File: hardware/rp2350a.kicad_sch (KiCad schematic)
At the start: 51 parts, among them Q2 DMN1150UFB-7B, Q7 DMN1150UFB-7B, U10 TXU0101DRYR, U32 TS2306A 240GF MSM 9_C2976675, U36 RP2354B_C39843328, X1 XTM25012000JT00351001

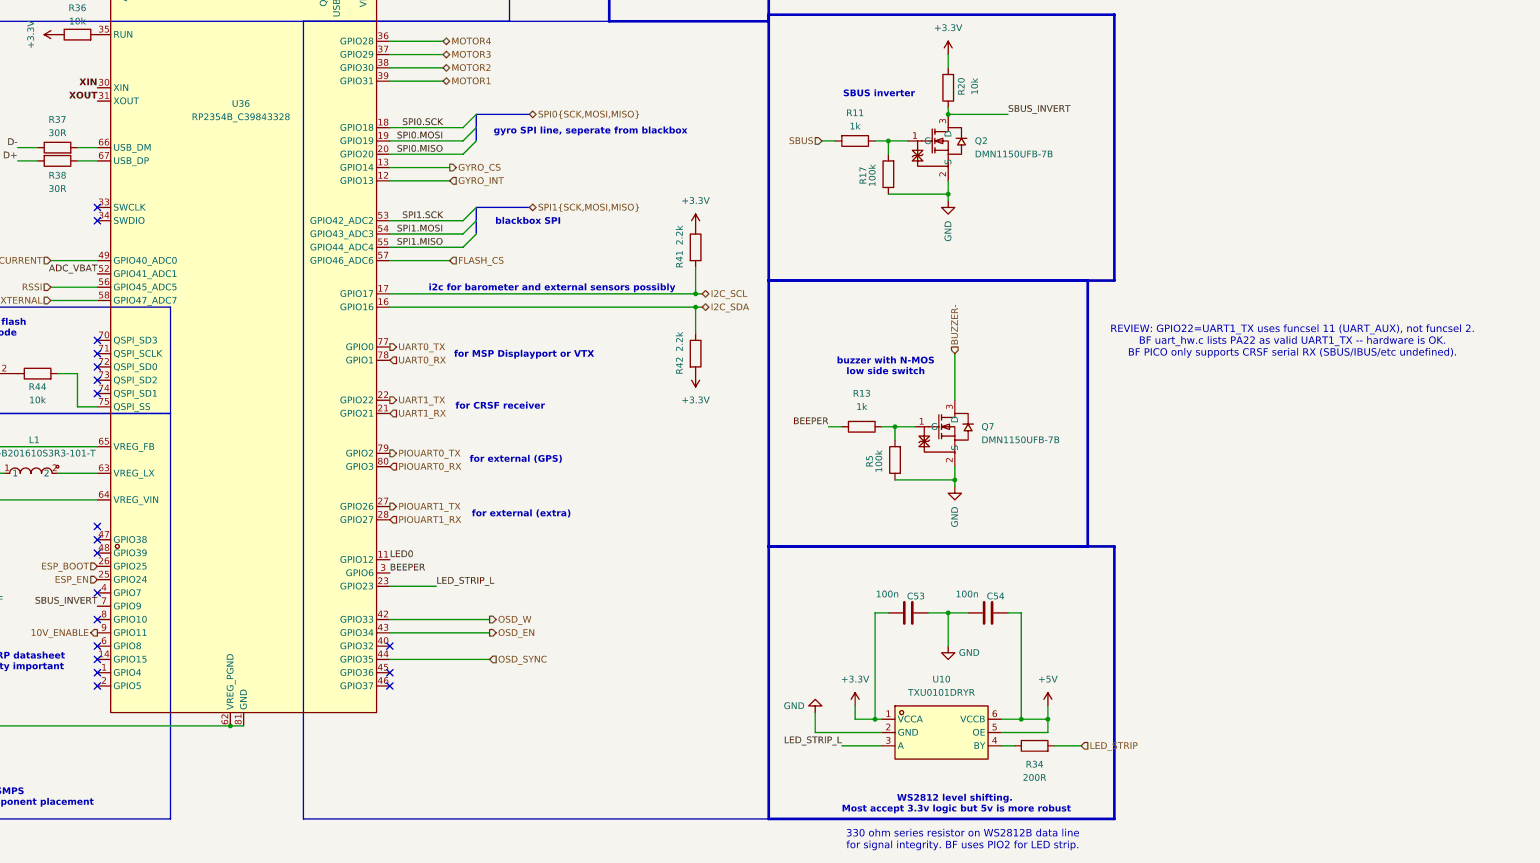
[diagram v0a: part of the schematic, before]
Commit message: Standardize repo: .gitignore, README, license, remove orphaned files
- Standardize .gitignore to match ecosystem template
- Fix README: correct GitHub URL, remove generic sections, remove nonexistent dirs
- Replace LICENSE stub with full CERN-OHL-S-2.0 text
- Remove orphaned schematics (baro, blackbox, compass, elrs, leds) — not in ECO variant
- Delete self-referential symlink and parent OpenFC production leftovers
- Add new footprints and 3D models (SIM, TF connectors)

Co-Authored-By: Claude Opus 4.6 (1M context) <noreply@anthropic.com>
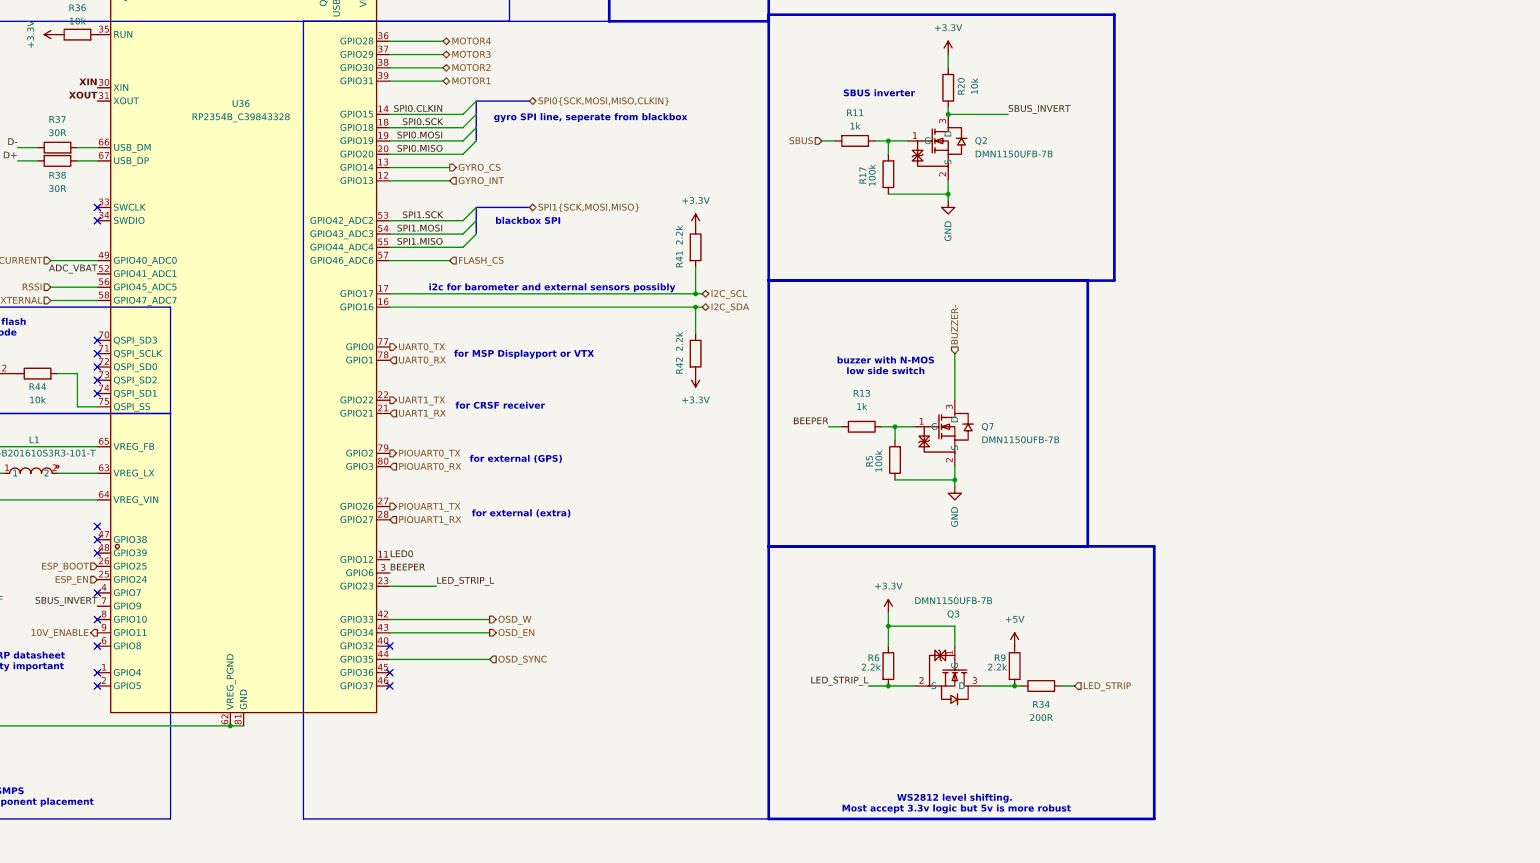
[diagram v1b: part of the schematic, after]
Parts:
- removed C53, C54: 100n, Capacitor_SMD:C_0201_0603Metric, symbol Device:C
- removed U10: TXU0101DRYR, lib:SON-6_L1.5-W1.0-P0.50-TL, symbol lib:TXU0101DRYR
- added Q3: DMN1150UFB-7B, lib:DFN-3L_L1.0-W0.6-P0.65-BR, symbol lib:DMN1150UFB-7B
- added R6, R9: 2.2k, Capacitor_SMD:C_0201_0603Metric, symbol Device:R
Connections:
- net +3.3V: now also Q3.1 (G), R6.1
- net +5V: now also R9.1
- net LED_STRIP_L: now also Q3.2 (S), R6.2
- net at R34.1: now also Q3.3 (D), R9.2
- net SPI0.CLKIN: now reaches U36.14 (GPIO15)
- no-connect marks 21 -> 20
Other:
- note removed: "330 ohm series resistor on WS2812B data line for signal integrity. BF uses PIO2 for LED strip."
- note removed: "REVIEW: GPIO22=UART1_TX uses funcsel 11 (UART_AUX), not funcsel 2. BF uart_hw.c lists PA22 as valid UART1_TX -- hardware is OK. BF PICO only supports CRSF serial RX (SBUS/IBUS/etc undefined)."
- moved on the sheet: R34

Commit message: WIP: schematic updates, library modernization, audit tooling
Schematic changes (user):
- Add ADC bypass caps on CURRENT/RSSI/EXTERNAL (1k + 100nF RC filter)
- Add IMU GYRO_CS 10k pull-up to +3.3V
- Reverse P1 ESC 8-pin JST SH pinout to BF standard
  (pin1=V+, pin2=GND, pin3=Current, pin5-8=M1-M4)
- SD card (blackbox) sub-sheet with SPI1 + FLASH_CS + decoupling
- Other sub-sheet cleanup (rp2350a, osd, pads, power, imu)

Footprint library:
- Convert all 62 legacy (module ...) footprints to modern
  (footprint ...) format via pcbnew API — fixes kicad-sch-api
  "footprint not found" errors

Tooling:
- Add hardware/tools/audit_design.py (BF-rule design audit script)
- Add hardware/tools/design_audit.md (audit report output)

Docs:
- Update CLAUDE.md: current GPIO map, corrected power tree net names,
  open issues list (CRIT-2..5), connector verification status

Co-Authored-By: Claude Opus 4.6 (1M context) <noreply@anthropic.com>
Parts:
- added C14, C15, C16, C22: 100n, Capacitor_SMD:C_0201_0603Metric, symbol Device:C
- added R15: 10k, Capacitor_SMD:C_0201_0603Metric, symbol Device:R
- added R6, R7, R8: 1k, Capacitor_SMD:C_0201_0603Metric, symbol Device:R
- renumbered C27 to C1, C73 to C10, C43 to C11, C44 to C12, C50 to C13, C51 to C17, C67 to C18, C52 to C19, C28 to C2, C68 to C20, C60 to C21, C62 to C23, C29 to C3, C56 to C4, C65 to C5, C59 to C6, C30 to C7, C31 to C8, C42 to C9, D8 to D1, Q2 to Q1, Q7 to Q2, R43 to R1, R36 to R10, R44 to R11, R37 to R12, R38 to R13, R56 to R14, R22 to R16, R41 to R17, R42 to R18, R11 to R19, R35 to R2, R13 to R20, R17 to R21, R6 to R22, R5 to R23, R20 to R24, R9 to R25, R34 to R26, R40 to R3, R39 to R4, R23 to R5, R55 to R9, U32 to U1, U36 to U2
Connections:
- net +3.3V: now also R15.2
- net ESC_CURRENT: now also C14.2, R6.2; no longer U2.49 (GPIO40_ADC0)
- net EXTERNAL: now also C16.2, R8.2; no longer U2.58 (GPIO47_ADC7)
- net GND: now also C14.1, C15.1, C16.1, C22.1
- net RSSI: now also C15.2, R7.2; no longer U2.56 (GPIO45_ADC5)
- net at R10.2, U2.35 (RUN): now also C22.2
- net ESP_BOOT: no longer names the net of U2.26 (GPIO25)
- net ESP_EN: no longer names the net of U2.25 (GPIO24)
- new net: R6.1, U2.49 (GPIO40_ADC0)
- new net: R8.1, U2.58 (GPIO47_ADC7)
- new net: R7.1, U2.56 (GPIO45_ADC5)
- no-connect marks 20 -> 22
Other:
- moved on the sheet: C4, R1, R10, R2

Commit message: V0.3 routed: pin remap, footprint fixes, EMC checklist, DFM prep
Schematic (user):
- OSD pins remapped to GPIO4-6 (OSD_W/OSD_EN/OSD_SYNC consecutive
  for FB_OSD PIO driver per BF PR#14882)
- SBUS inverter stays on GPIO9 (valid UART1_RX)
- Beeper moved to GPIO36
- Various sub-sheet updates

PCB:
- Full board routed, bottom-side component placement
- Resistor footprints: C_0201 -> R_0201 for correct 3D models
- Capacitor 3D model paths fixed (were pointing to R_0201)
- SD card footprint 3D path fixed (${KIPRJMOD}/lib.3dshapes/)
- 2 footprint 3D paths fixed (SIM, TF-01A: /lib.3dshapes -> ${KIPRJMOD})

Tooling & docs:
- Add EMC checklist (hardware/tools/EMC_CHECKLIST.md)
- Add EMC note script (hardware/tools/add_emc_note.py)
- Update CLAUDE.md: LMR51430 drop-in upgrade noted, connector
  verification, OSD pin mapping

Co-Authored-By: Claude Opus 4.6 (1M context) <noreply@anthropic.com>
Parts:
- R1, R10, R11, R12, R13, R14, R15, R16, R17, R18, R19, R2, R20, R21, R22, R23, R24, R25, R26, R3, R4, R5, R6, R7, R8, R9: footprint Capacitor_SMD:C_0201_0603Metric -> Resistor_SMD:R_0201_0603Metric
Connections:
- net BEEPER: now also U2.4 (GPIO7); no longer U2.3 (GPIO6)
- net GYRO_CS: now also R15.1
- net OSD_EN: now also U2.2 (GPIO5); no longer U2.43 (GPIO34)
- net OSD_SYNC: now also U2.3 (GPIO6); no longer U2.44 (GPIO35)
- net OSD_W: now also U2.1 (GPIO4); no longer U2.42 (GPIO33)
- no-connect marks 22 -> 19
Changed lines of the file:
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@@
 	)
 	(junction
+		(at 280.67 120.65)
+		(diameter 0)
+		(color 0 0 0 0)
+	)
+	(junction
 		(at 361.95 125.73)
 		(diameter 0)
@@
 	)
 	(no_connect
-		(at 199.39 217.17)
-	)
-	(no_connect
 		(at 255.27 212.09)
 	)
@@
 	)
 	(no_connect
-		(at 199.39 201.93)
-	)
-	(no_connect
 		(at 199.39 212.09)
 	)
@@
 	)
 	(no_connect
-		(at 199.39 219.71)
-	)
-	(no_connect
 		(at 199.39 156.21)
 	)
@@
 	(wire
 		(pts
-			(xy 255.27 120.65) (xy 290.83 120.65)
+			(xy 255.27 120.65) (xy 280.67 120.65)
 		)
 		(stroke
@@
 	(wire
 		(pts
-			(xy 255.27 209.55) (xy 274.32 209.55)
-		)
-		(stroke
-			(width 0)
-			(type default)
-		)
-	)
-	(wire
-		(pts
 			(xy 361.95 125.73) (xy 361.95 127)
 		)
@@
 	(wire
 		(pts
-			(xy 255.27 214.63) (xy 274.32 214.63)
-		)
-		(stroke
-			(width 0)
-			(type default)
-		)
-	)
-	(wire
-		(pts
 			(xy 363.22 180.34) (xy 363.22 181.61)
 		)
@@
 	(wire
 		(pts
-			(xy 255.27 207.01) (xy 274.32 207.01)
+			(xy 269.24 71.12) (xy 269.24 74.93)
 		)
 		(stroke
@@
 	(wire
 		(pts
-			(xy 269.24 71.12) (xy 269.24 74.93)
+			(xy 166.37 110.49) (xy 166.37 143.51)
 		)
 		(stroke
@@
 	(wire
 		(pts
-			(xy 166.37 110.49) (xy 166.37 143.51)
+			(xy 124.46 72.39) (xy 124.46 77.47)
 		)
 		(stroke
@@
 	(wire
 		(pts
-			(xy 124.46 72.39) (xy 124.46 77.47)
+			(xy 255.27 147.32) (xy 313.69 147.32)
 		)
 		(stroke
@@
 	(wire
 		(pts
-			(xy 255.27 147.32) (xy 313.69 147.32)
+			(xy 224.79 76.2) (xy 227.33 76.2)
 		)
 		(stroke
@@
 	(wire
 		(pts
-			(xy 224.79 76.2) (xy 227.33 76.2)
+			(xy 280.67 120.65) (xy 290.83 120.65)
 		)
 		(stroke
@@
 	)
 	(label "BEEPER"
-		(at 255.27 198.12 0)
+		(at 199.39 201.93 180)
 		(effects
 			(font
 				(size 1.27 1.27)
 			)
-			(justify left bottom)
+			(justify right bottom)
 		)
 	)
@@
 		)
 	)
-	(hierarchical_label "OSD_SYNC"
-		(shape input)
-		(at 274.32 214.63 0)
-		(effects
-			(font
-				(size 1.27 1.27)
-			)
-			(justify left)
-		)
-	)
 	(hierarchical_label "I2C_SCL"
 		(shape bidirectional)
@@
 		)
 	)
-	(hierarchical_label "OSD_W"
-		(shape output)
-		(at 274.32 207.01 0)
-		(effects
-			(font
-				(size 1.27 1.27)
-			)
-			(justify left)
-		)
-	)
 	(hierarchical_label "EXTERNAL"
 		(shape input)
@@
 		)
 	)
+	(hierarchical_label "OSD_W"
+		(shape output)
+		(at 199.39 217.17 180)
+		(effects
+			(font
+				(size 1.27 1.27)
+			)
+			(justify right)
+		)
+	)
 	(hierarchical_label "SPI1{SCK,MOSI,MISO}"
 		(shape bidirectional)
@@
 		)
 	)
-	(hierarchical_label "OSD_EN"
-		(shape output)
-		(at 274.32 209.55 0)
-		(effects
-			(font
-				(size 1.27 1.27)
-			)
-			(justify left)
-		)
-	)
 	(hierarchical_label "SBUS"
 		(shape input)
@@
 		)
 	)
+	(hierarchical_label "OSD_SYNC"
+		(shape input)
+		(at 255.27 198.12 0)
+		(effects
+			(font
+				(size 1.27 1.27)
+			)
+			(justify left)
+		)
+	)
 	(hierarchical_label "PIOUART1_RX"
 		(shape input)
@@
 		)
 	)
+	(hierarchical_label "OSD_EN"
+		(shape output)
+		(at 199.39 219.71 180)
+		(effects
+			(font
+				(size 1.27 1.27)
+			)
+			(justify right)
+		)
+	)
 	(hierarchical_label "PIOUART0_TX"
 		(shape output)
@@
 			)
 		)
-		(property "Footprint" "Capacitor_SMD:C_0201_0603Metric"
+		(property "Footprint" "Resistor_SMD:R_0201_0603Metric"
 			(at 379.73 221.488 90)
 			(hide yes)
@@
 			)
 		)
-		(property "Footprint" "Capacitor_SMD:C_0201_0603Metric"
+		(property "Footprint" "Resistor_SMD:R_0201_0603Metric"
 			(at 353.568 176.53 90)
 			(hide yes)
@@
 			)
 		)
-		(property "Footprint" "Capacitor_SMD:C_0201_0603Metric"
+		(property "Footprint" "Resistor_SMD:R_0201_0603Metric"
 			(at 191.77 118.618 90)
 			(hide yes)
@@
 			)
 		)
-		(property "Footprint" "Capacitor_SMD:C_0201_0603Metric"
+		(property "Footprint" "Resistor_SMD:R_0201_0603Metric"
 			(at 78.74 206.502 90)
 			(hide yes)
@@
 			)
 		)
-		(property "Footprint" "Capacitor_SMD:C_0201_0603Metric"
+		(property "Footprint" "Resistor_SMD:R_0201_0603Metric"
 			(at 345.44 168.402 90)
 			(hide yes)
@@
 			)
 		)
-		(property "Footprint" "Capacitor_SMD:C_0201_0603Metric"
+		(property "Footprint" "Resistor_SMD:R_0201_0603Metric"
 			(at 344.17 113.792 90)
 			(hide yes)
@@
 			)
 		)
-		(property "Footprint" "Capacitor_SMD:C_0201_0603Metric"
+		(property "Footprint" "Resistor_SMD:R_0201_0603Metric"
 			(at 372.872 215.9 90)
 			(hide yes)
@@
 			)
 		)
-		(property "Footprint" "Capacitor_SMD:C_0201_0603Metric"
+		(property "Footprint" "Resistor_SMD:R_0201_0603Metric"
 			(at 78.74 221.742 90)
 			(hide yes)
@@
 			)
 		)
-		(property "Footprint" "Capacitor_SMD:C_0201_0603Metric"
+		(property "Footprint" "Resistor_SMD:R_0201_0603Metric"
 			(at 53.34 112.268 90)
 			(hide yes)
@@
 			)
 		)
-		(property "Footprint" "Capacitor_SMD:C_0201_0603Metric"
+		(property "Footprint" "Resistor_SMD:R_0201_0603Metric"
 			(at 282.448 116.84 90)
 			(hide yes)
@@
 			)
 		)
-		(property "Footprint" "Capacitor_SMD:C_0201_0603Metric"
+		(property "Footprint" "Resistor_SMD:R_0201_0603Metric"
 			(at 352.298 121.92 90)
 			(hide yes)
@@
 			)
 		)
-		(property "Footprint" "Capacitor_SMD:C_0201_0603Metric"
+		(property "Footprint" "Resistor_SMD:R_0201_0603Metric"
 			(at 311.912 135.89 90)
 			(hide yes)
@@
 			)
 		)
-		(property "Footprint" "Capacitor_SMD:C_0201_0603Metric"
+		(property "Footprint" "Resistor_SMD:R_0201_0603Metric"
 			(at 348.742 215.9 90)
 			(hide yes)
@@
 			)
 		)
-		(property "Footprint" "Capacitor_SMD:C_0201_0603Metric"
+		(property "Footprint" "Resistor_SMD:R_0201_0603Metric"
 			(at 53.34 103.378 90)
 			(hide yes)
@@
 			)
 		)
-		(property "Footprint" "Capacitor_SMD:C_0201_0603Metric"
+		(property "Footprint" "Resistor_SMD:R_0201_0603Metric"
 			(at 144.78 88.392 90)
 			(hide yes)
@@
 			)
 		)
-		(property "Footprint" "Capacitor_SMD:C_0201_0603Metric"
+		(property "Footprint" "Resistor_SMD:R_0201_0603Metric"
 			(at 144.78 127.762 90)
 			(hide yes)
@@
 			)
 		)
-		(property "Footprint" "Capacitor_SMD:C_0201_0603Metric"
+		(property "Footprint" "Resistor_SMD:R_0201_0603Metric"
 			(at 267.462 63.5 90)
 			(hide yes)
@@
 			)
 		)
-		(property "Footprint" "Capacitor_SMD:C_0201_0603Metric"
+		(property "Footprint" "Resistor_SMD:R_0201_0603Metric"
 			(at 183.642 63.5 90)
 			(hide yes)
@@
 			)
 		)
-		(property "Footprint" "Capacitor_SMD:C_0201_0603Metric"
+		(property "Footprint" "Resistor_SMD:R_0201_0603Metric"
 			(at 305.562 60.96 90)
 			(hide yes)
@@
 			)
 		)
-		(property "Footprint" "Capacitor_SMD:C_0201_0603Metric"
+		(property "Footprint" "Resistor_SMD:R_0201_0603Metric"
 			(at 311.912 156.21 90)
 			(hide yes)
@@
 			)
 		)
-		(property "Footprint" "Capacitor_SMD:C_0201_0603Metric"
+		(property "Footprint" "Resistor_SMD:R_0201_0603Metric"
 			(at 120.65 164.592 90)
 			(hide yes)
@@
 			)
 		)
-		(property "Footprint" "Capacitor_SMD:C_0201_0603Metric"
+		(property "Footprint" "Resistor_SMD:R_0201_0603Metric"
 			(at 185.42 97.028 90)
 			(hide yes)
@@
 			)
 		)
-		(property "Footprint" "Capacitor_SMD:C_0201_0603Metric"
+		(property "Footprint" "Resistor_SMD:R_0201_0603Metric"
 			(at 363.728 105.41 90)
 			(hide yes)
@@
 			)
 		)
-		(property "Footprint" "Capacitor_SMD:C_0201_0603Metric"
+		(property "Footprint" "Resistor_SMD:R_0201_0603Metric"
 			(at 187.96 161.798 90)
 			(hide yes)
@@
 			)
 		)
-		(property "Footprint" "Capacitor_SMD:C_0201_0603Metric"
+		(property "Footprint" "Resistor_SMD:R_0201_0603Metric"
 			(at 191.77 117.602 90)
 			(hide yes)
@@
 			)
 		)
-		(property "Footprint" "Capacitor_SMD:C_0201_0603Metric"
+		(property "Footprint" "Resistor_SMD:R_0201_0603Metric"
 			(at 144.78 108.712 90)
 			(hide yes)

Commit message: Rev 2: fit 3A bucks, resolve power/LED/signal change-list items
Schematic (power, rp2350a) + docs in sync with Rev 2 decisions:

Power
- U3/U4 bucks: LMR51420 (2A) -> LMR51430YFDDCR (3A, C5219261)
- 10V FB R30 -> 6.49k (E96 stock) => Vout 9.85V
- C28 10V output cap kept 22uF 16V X5R 0603 (digital-VTX rail)
- L2/L3 both rails 4.7uH (XRTC303020D4R7MBCA)
- U6 gyro LDO kept NCV8187 (300mA) for PSRR

MCU/USB
- R12/R13/R14 kept at 30R (DFM consolidation, no impact)
- D1 USB ESD removed on schematic; flagged for restore (recommendation)

LEDs
- D2 LED0 -> blue XL-1005UBC; greens XL-1005UGC; all 0402
- Series resistors recalculated for ~1mA: D2 510R, D7 680R, D5 2.4k, D4 7.5k

Signals/decisions
- SBUS hardware inverter removed (BF PICO inverts at the RP2350 pad)
- Beeper done: N-MOS low-side (Q2 DMN1150UFB-7B)
- SDIO blackbox: stay on SPI (Betaflight PICO has no SDIO support)
- CRIT-2 motor order: keep reversed silk, fix in BF target resource map
- U5 confirmed TPS2116; SWD connector not added

Ignore generated analysis/ dump.

Co-Authored-By: Claude Opus 4.8 (1M context) <noreply@anthropic.com>
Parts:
- removed D1: USBLC6-2P6, Package_TO_SOT_SMD:SOT-666, symbol lib:USBLC6-2SC6
- removed Q1: DMN1150UFB-7B, lib:DFN-3L_L1.0-W0.6-P0.65-BR, symbol lib:DMN1150UFB-7B
- removed R19: 1k, Resistor_SMD:R_0201_0603Metric, symbol Device:R
- removed R21: 100k, Resistor_SMD:R_0201_0603Metric, symbol Device:R
- removed R24: 10k, Resistor_SMD:R_0201_0603Metric, symbol Device:R
- D2: value LED_1_Green -> LED_1_Blue; footprint LED_SMD:LED_0201_0603Metric -> LED_SMD:LED_0402_1005Metric; LCSC C3646922 -> C22355736; MPN XL-0201UGC -> XL-1005UBC
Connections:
- net SBUS_INVERT is gone; now on net SBUS: U2.7 (GPIO9)
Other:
- note removed: "SBUS inverter"
